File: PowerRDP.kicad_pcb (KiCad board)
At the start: 2 copper layers, 41.3 x 33.7 mm, 27 parts, among them J1 Conn_01x02_Male, J2 Conn_01x02_Male, J3 Conn_01x02_Male, J4 Conn_01x02_Male, J5 Conn_01x02_Male, J6 Conn_01x02_Male, J7 Conn_01x02_Male, J8 Conn_01x02_Male, J9 Conn_01x03_Male, U2 KA378R12C, U3 AZ1117CH-3.3, U4 MEA1D1515SC

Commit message: Increment revison
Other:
- board text added: "HELEN RDP Power Board Rev02"
- board text removed: "HELEN RDP Power Board Rev01"
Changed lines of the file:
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@@
     (arrow2b (pts (xy 120.65 39.37) (xy 121.776504 38.783579)))
   )
-  (gr_text "HELEN RDP Power Board Rev01" (at 137.16 71.12 90) (layer F.SilkS)
+  (gr_text "HELEN RDP Power Board Rev02" (at 140.97 69.85) (layer F.SilkS)
     (effects (font (size 0.8 0.8) (thickness 0.2)))
   )

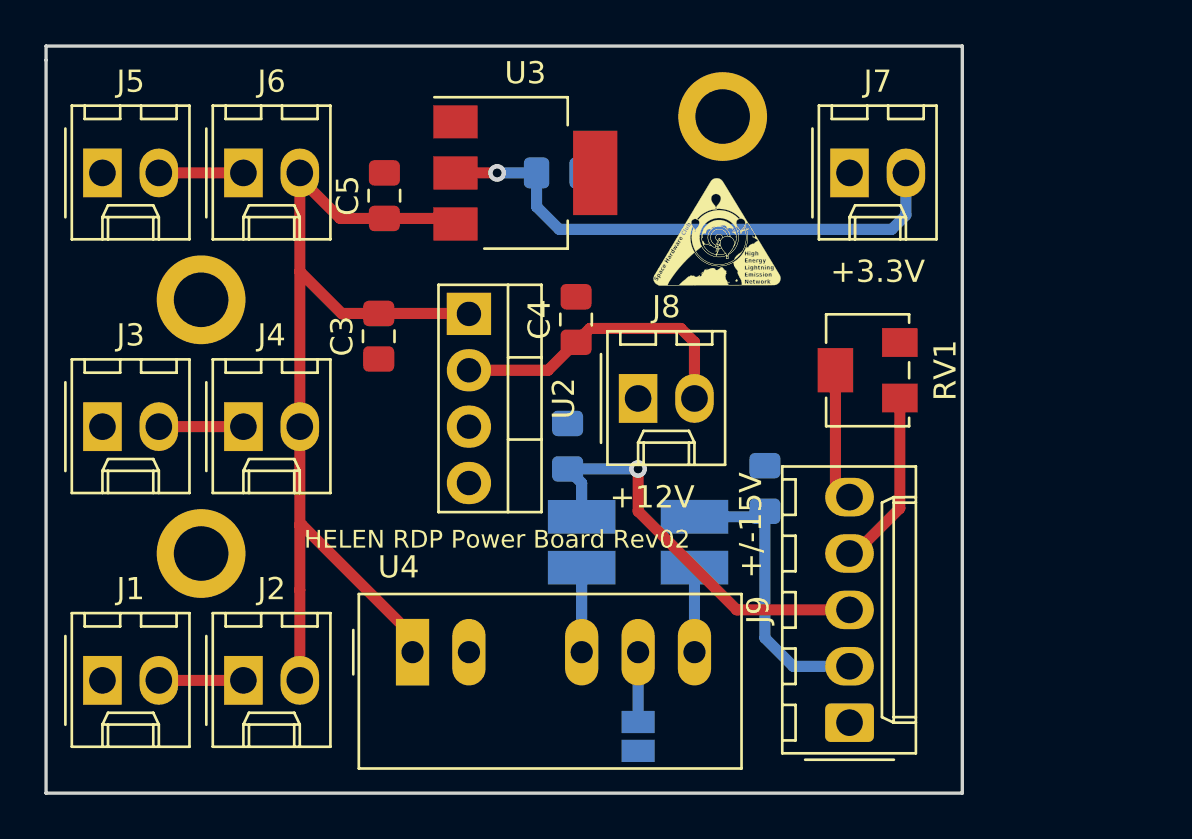
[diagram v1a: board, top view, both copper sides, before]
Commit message: Fix 15V regulator, add blinking FAA LEDs
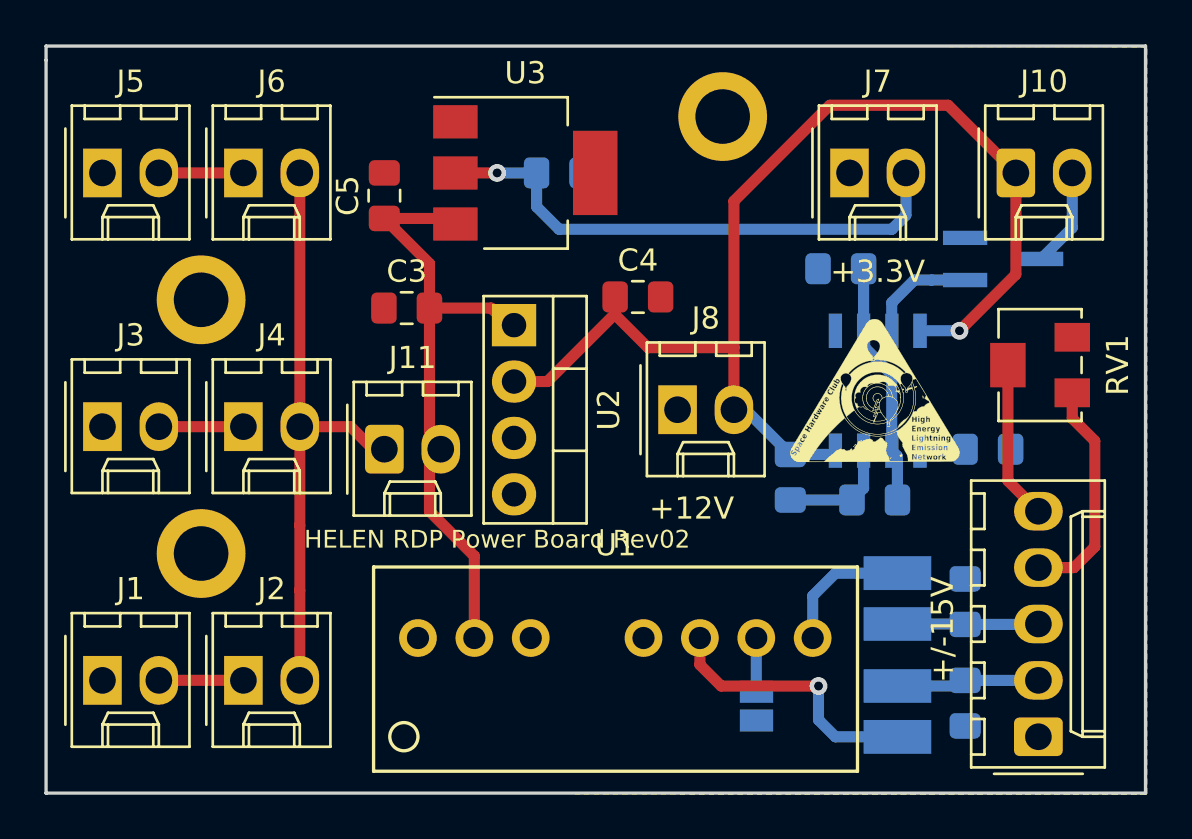
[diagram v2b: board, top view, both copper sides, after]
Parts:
- removed the G*** at (150.9, 55.9)
- added C7: .01 uF, Capacitor_SMD:C_0805_2012Metric_Pad1.15x1.40mm_HandSolder, B.Cu at (163.1, 65.8)
- added C8: 47 uF, Capacitor_SMD:C_0805_2012Metric_Pad1.15x1.40mm_HandSolder, B.Cu at (156.5, 57.7)
- added G***: LOGO, rdplibs:HELENlogo_large, F.Cu at (158.0, 63.0)
- added J10: FAA LED, Connector_Molex:Molex_KK-254_AE-6410-02A_1x02_P2.54mm_Vertical, F.Cu at (164.3, 53.3)
- added J11: Switch, Connector_Molex:Molex_KK-254_AE-6410-02A_1x02_P2.54mm_Vertical, F.Cu at (135.9, 65.8)
- added Q1: NTR4003NT1G, Package_TO_SOT_SMD:TSOT-23_HandSoldering, B.Cu at (163.8, 57.2)
- added R1: 3k, Resistor_SMD:R_0805_2012Metric_Pad1.15x1.40mm_HandSolder, B.Cu at (158.0, 68.1)
- added R2: 24k, Resistor_SMD:R_0805_2012Metric_Pad1.15x1.40mm_HandSolder, B.Cu at (154.2, 67.0)
- added U1: Recom_RS3, PowerRDP:Recom_RS3, F.Cu at (146.3, 75.7)
- J7: value Conn_01x02_Male -> 3.3V
- J8: value Conn_01x02_Male -> 12V
- J9: value Conn_01x03_Male -> FPGA
- U4: value MEA1D1515SC -> TS555; footprint Converter_DCDC:Converter_DCDC_TRACO_TMR-1-xxxx_Dual_THT -> Package_SO:SOIC-8_3.9x4.9mm_P1.27mm; moved to B.Cu
- moved U4 24.0 mm to (158.1, 63.2), turned to 270 degrees
- moved C1 19.2 mm to (162.1, 72.7)
- moved L1 14.4 mm to (159.0, 72.5), turned to 270 degrees
- moved C2 13.2 mm to (162.1, 77.2), turned to 270 degrees
- moved L2 11.9 mm to (159.0, 77.6)
- moved J9 8.53 mm to (165.4, 78.7)
- moved RV1 7.77 mm to (165.4, 62.0)
- moved JP1 5.51 mm to (152.7, 77.4)
- moved C4 2.96 mm to (147.3, 58.9), turned to 0 degrees
- moved U2 2.09 mm to (141.7, 60.2)
- moved J8 1.85 mm to (149.1, 64.0)
- moved C3 1.79 mm to (136.9, 59.4), turned to 0 degrees
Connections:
- C3 pad 2: +BATT -> /POWR
- C5 pad 1: +BATT -> /POWR
- U2 pad 1: +BATT -> /POWR
- U3 pad 3: +BATT -> /POWR
- U4 pad 1: +BATT -> GND
- U4 pad 2: GND -> /THR
- U4 pad 4: Net-(L1-Pad1) -> /+12V
- U4 pad 5: Net-(JP1-Pad1) -> Net-(C7-Pad1)
- U4 pad 6: Net-(L2-Pad1) -> /THR
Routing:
- net /+12V: track 13.7 -> 53.9 mm, vias 0 -> 1
- net /POWR: track 0.00 -> 27.8 mm
- net +BATT: track 70.1 -> 49.7 mm
- net /-15V: track 18.9 -> 6.36 mm, vias 1 -> 0
- net /THR: track 0.00 -> 11.0 mm
- net Net-(L2-Pad1): track 3.81 -> 12.3 mm, vias 0 -> 1
- net /+15V: track 13.3 -> 6.46 mm
- net Net-(R1-Pad1): track 0.00 -> 5.21 mm
- net /FAA_SIG: track 0.00 -> 5.00 mm
- net /FAA_GND: track 0.00 -> 4.46 mm
- net Net-(L1-Pad1): track 3.81 -> 6.14 mm
- net /C_in: track 8.08 -> 10.3 mm
- net Net-(C7-Pad1): track 0.00 -> 2.06 mm
- net /C_out: track 5.98 -> 7.15 mm
- net Net-(JP1-Pad1): track 3.14 -> 2.42 mm
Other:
- board size 41.3 x 33.7 mm -> 49.5 x 33.7 mm
- board text removed: "-"

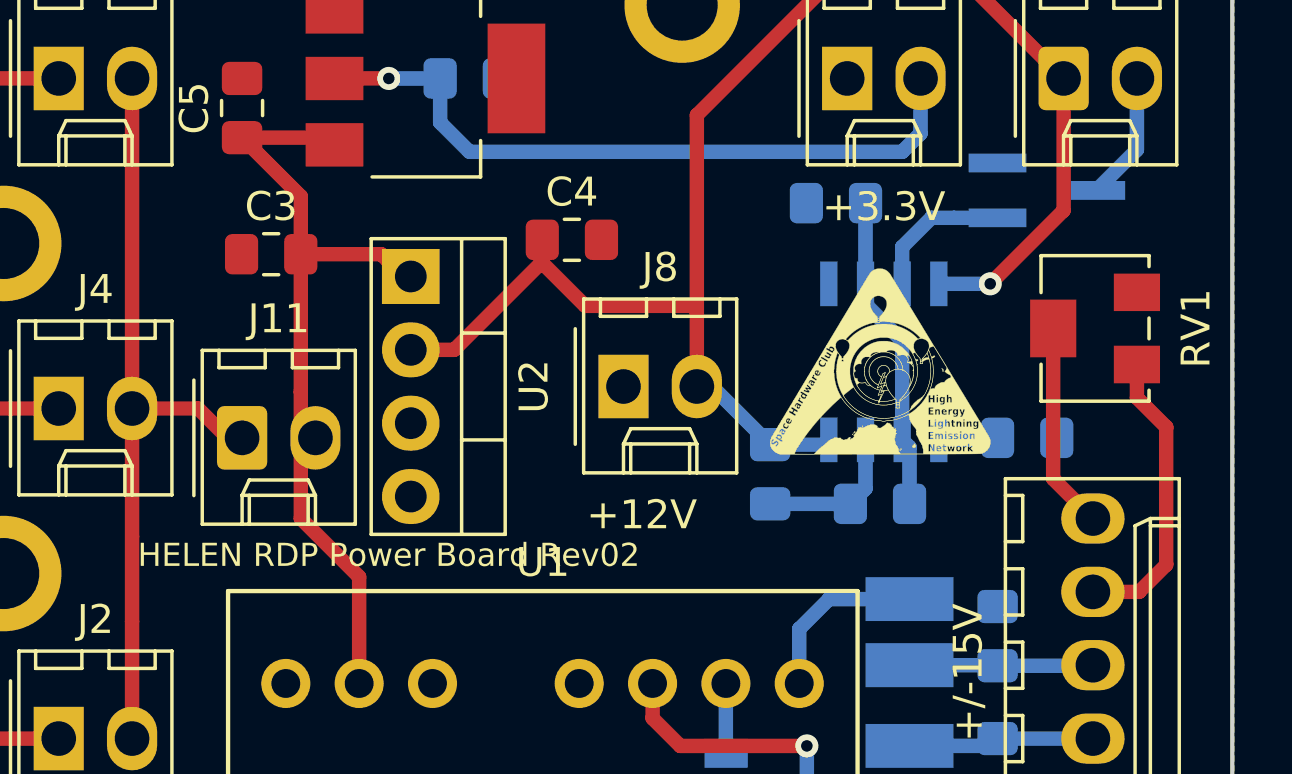
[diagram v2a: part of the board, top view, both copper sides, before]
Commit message: Add silkscreen labels to connectors
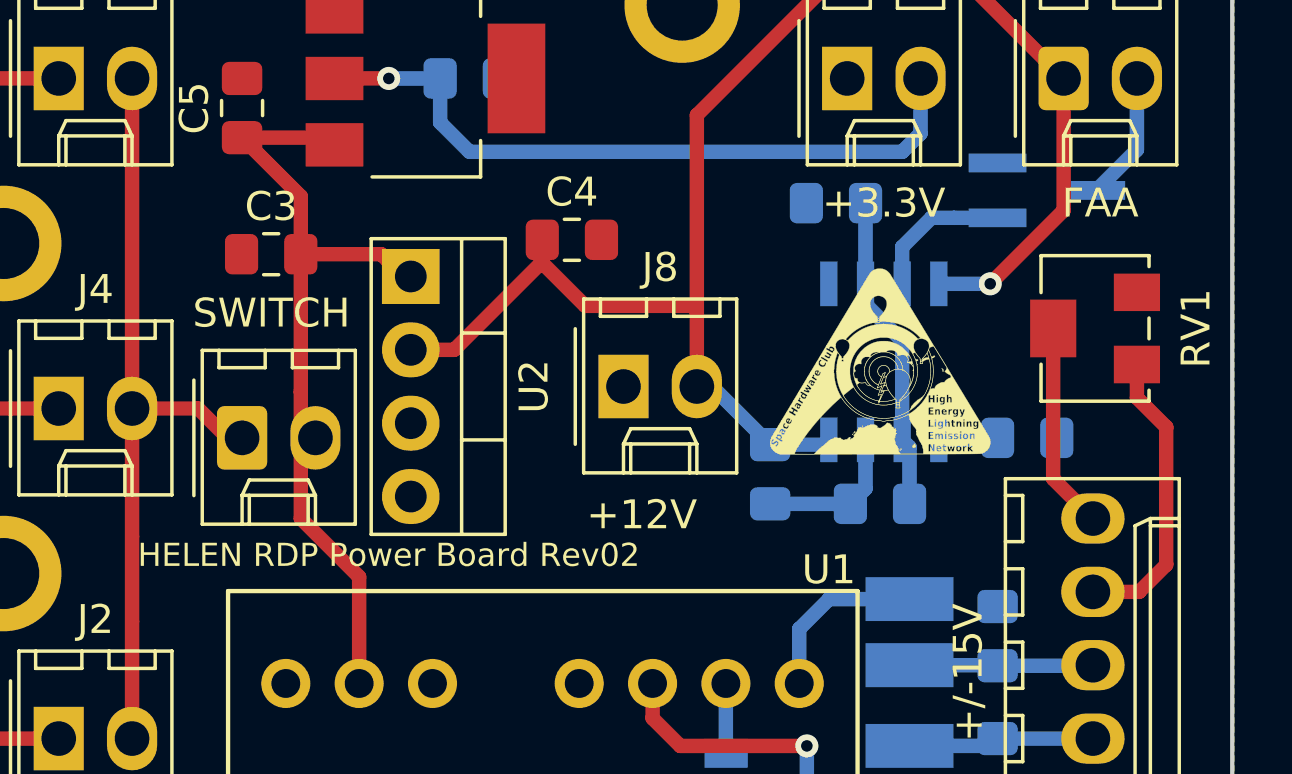
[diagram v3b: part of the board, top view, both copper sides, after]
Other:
- board text added: "FAA"
- board text added: "SWITCH"
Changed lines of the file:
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@@
   (general
     (thickness 1.6)
-    (drawings 16)
+    (drawings 18)
     (tracks 97)
     (zones 0)
@@
     (descr "Molex KK-254 Interconnect System, old/engineering part number: AE-6410-02A example for new part number: 22-27-2021, 2 Pins (http://www.molex.com/pdm_docs/sd/022272021_sd.pdf), generated with kicad-footprint-generator")
     (tags "connector Molex KK-254 side entry")
-    (fp_text reference J11 (at 1.27 -4.12) (layer F.SilkS)
+    (fp_text reference J11 (at 1.27 -4.12) (layer F.SilkS) hide
       (effects (font (size 1 1) (thickness 0.15)))
     )
@@
   (module PowerRDP:Recom_RS3 (layer F.Cu)
     (at 146.304 75.692)
-    (fp_text reference U1 (at 0 -5.588) (layer F.SilkS)
+    (fp_text reference U1 (at 9.906 -5.334) (layer F.SilkS)
       (effects (font (size 1 1) (thickness 0.15)))
     )
@@
       (xy 0.017454 -3.065725)) (layer F.SilkS) (width 0.01))
   )
+  (gr_text FAA (at 165.608 57.658) (layer F.SilkS)
+    (effects (font (size 1 1) (thickness 0.2)))
+  )
+  (gr_text "SWITCH\n" (at 136.906 61.468) (layer F.SilkS)
+    (effects (font (size 1 1) (thickness 0.2)))
+  )
   (gr_text + (at 168.402 75.946) (layer B.SilkS)
     (effects (font (size 1 1) (thickness 0.2)) (justify mirror))
@@
     (effects (font (size 1 1) (thickness 0.2)))
   )
-  (gr_text +3.3V (at 158.115 57.785) (layer F.SilkS)
+  (gr_text +3.3V (at 158.115 57.658) (layer F.SilkS)
     (effects (font (size 1 1) (thickness 0.2)))
   )

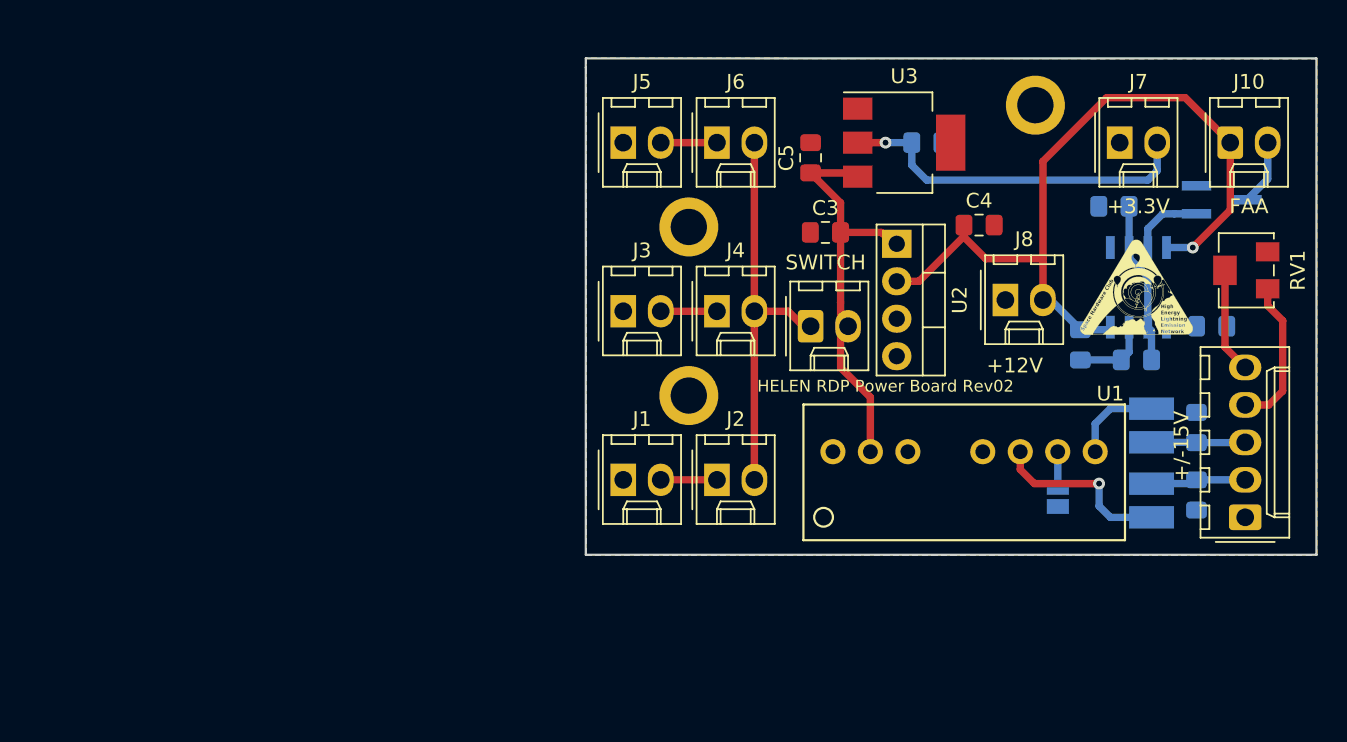
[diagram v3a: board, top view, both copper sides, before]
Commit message: Remake power board with updated single-output regulators. PCB entirely redesigned
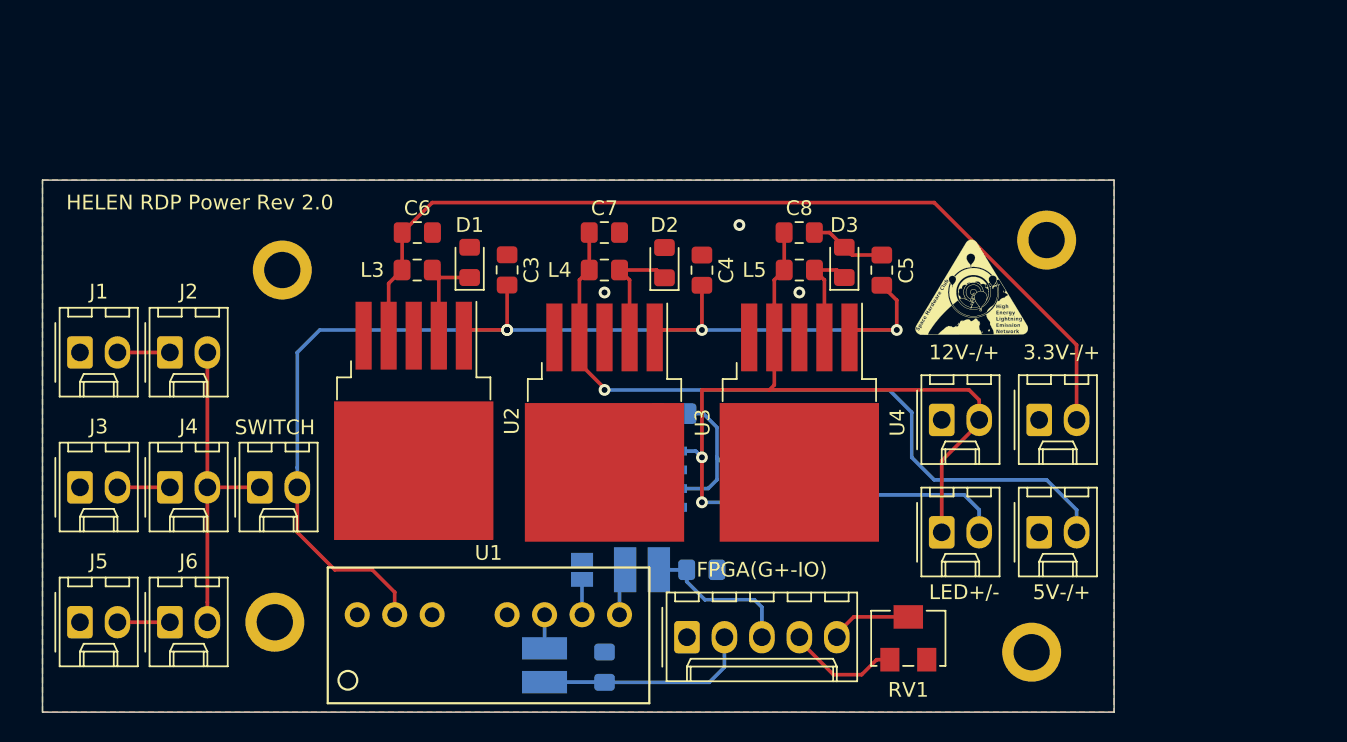
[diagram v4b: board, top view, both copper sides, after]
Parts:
- removed the G*** at (135.6, 62.7)
- removed the REF** at (151.1, 50.8)
- removed the REF** at (127.6, 70.5)
- removed the REF** at (127.6, 59.1)
- added C10: 47 uF, Capacitor_SMD:C_0805_2012Metric_Pad1.15x1.40mm_HandSolder, B.Cu at (126.6, 71.7)
- added C9: .01 uF, Capacitor_SMD:C_0805_2012Metric_Pad1.15x1.40mm_HandSolder, B.Cu at (123.4, 79.2)
- added D1: 1N5819, Diode_SMD:D_0805_2012Metric_Pad1.15x1.40mm_HandSolder, F.Cu at (112.8, 61.5)
- added D2: 1N5819, Diode_SMD:D_0805_2012Metric_Pad1.15x1.40mm_HandSolder, F.Cu at (126.0, 61.5)
- added D3: 1N5819, Diode_SMD:D_0805_2012Metric_Pad1.15x1.40mm_HandSolder, F.Cu at (138.2, 61.5)
- added G***: LOGO, rdplibs:GP2image, F.Cu at (103.6, 74.7)
- added J12: Switch, Connector_Molex:Molex_KK-254_AE-6410-02A_1x02_P2.54mm_Vertical, F.Cu at (98.6, 76.7)
- added L3: 330uH, Inductor_SMD:L_0805_2012Metric_Pad1.15x1.40mm_HandSolder, F.Cu at (109.2, 62.0)
- added L4: 330uH, Inductor_SMD:L_0805_2012Metric_Pad1.15x1.40mm_HandSolder, F.Cu at (121.9, 62.0)
- added L5: 330uH, Inductor_SMD:L_0805_2012Metric_Pad1.15x1.40mm_HandSolder, F.Cu at (135.1, 62.0)
- added REF**: ScrewHole, rdplibs:ScrewHole, F.Cu at (99.6, 85.9)
- added REF**: ScrewHole, rdplibs:ScrewHole, F.Cu at (100.1, 62.0)
- added REF**: ScrewHole, rdplibs:ScrewHole, F.Cu at (151.9, 59.9)
- added REF**: ScrewHole, rdplibs:ScrewHole, F.Cu at (150.9, 87.9)
- added U5: TS555, Package_SO:SOIC-8_3.9x4.9mm_P1.27mm, B.Cu at (129.4, 76.2)
- C3, C5: value 10 uF -> 100uF
- C4: value 47 uF -> 100uF
- C6: value 22 uF -> 330uF; moved to F.Cu
- C7: value .01 uF -> 330uF; moved to F.Cu
- C8: value 47 uF -> 330uF; moved to F.Cu
- J10: value FAA LED -> FPGA; footprint Connector_Molex:Molex_KK-254_AE-6410-02A_1x02_P2.54mm_Vertical -> Connector_Molex:Molex_KK-254_AE-6410-05A_1x05_P2.54mm_Vertical
- J11: value Switch -> FAA LED
- J8: value 12V -> 5V
- J9: value FPGA -> 12V; footprint Connector_Molex:Molex_KK-254_AE-6410-05A_1x05_P2.54mm_Vertical -> Connector_Molex:Molex_KK-254_AE-6410-02A_1x02_P2.54mm_Vertical
- U2: value KA378R12C -> LM2575-3.3BU; footprint Package_TO_SOT_THT:TO-220-4_Vertical -> Package_TO_SOT_SMD:TO-263-5_TabPin3
- U3: value AZ1117CH-3.3 -> LM2575-5.0BU; footprint Package_TO_SOT_SMD:SOT-223 -> Package_TO_SOT_SMD:TO-263-5_TabPin3
- U4: value TS555 -> LM2575-12BU; footprint Package_SO:SOIC-8_3.9x4.9mm_P1.27mm -> Package_TO_SOT_SMD:TO-263-5_TabPin3; moved to F.Cu
- moved J10 49.8 mm to (127.5, 86.9)
- moved J6 49.3 mm to (92.5, 85.9)
- moved J5 49.1 mm to (86.4, 85.9)
- moved L2 42.6 mm to (117.9, 88.8), turned to 270 degrees
- moved C2 41.8 mm to (121.9, 88.9), turned to 90 degrees
- moved C7 41.7 mm to (121.9, 59.4)
- moved J4 39.0 mm to (92.5, 76.7)
- moved J3 38.7 mm to (86.4, 76.7)
- moved J2 38.1 mm to (92.5, 67.6)
- moved J1 37.8 mm to (86.4, 67.6)
- moved L1 35.9 mm to (124.5, 82.3), turned to 0 degrees
- moved R2 35.7 mm to (119.4, 75.3), turned to 0 degrees
- moved R1 35.4 mm to (123.5, 76.3), turned to 270 degrees
- moved C6 35.1 mm to (109.2, 59.4)
- moved C1 34.9 mm to (128.5, 82.3), turned to 0 degrees
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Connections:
- C4 pad 1: /+12V -> GND
- C4 pad 2: GND -> /POWR
- C5 pad 1: /POWR -> GND
- C5 pad 2: GND -> /POWR
- C7 pad 1: Net-(C7-Pad1) -> /+5V
- C8 pad 1: /THR -> /+12V
- J10 pad 1: /+12V -> GND
- J10 pad 2: /FAA_GND -> /+15V
- J11 pad 1: +BATT -> /+12V
- J11 pad 2: /POWR -> /FAA_GND
- J8 pad 2: /+12V -> /+5V
- J9 pad 2: /+15V -> /+12V
- U2 pad 2: /+12V -> Net-(D1-Pad1)
- U2 pad 4: Net-(U2-Pad4) -> /+3.3V
- U3 pad 1: GND -> /POWR
- U3 pad 2: /+3.3V -> Net-(D2-Pad1)
- U3 pad 3: /POWR -> GND
- U3 pad 4: (no net) -> /+5V
- U4 pad 1: GND -> /POWR
- U4 pad 2: /THR -> Net-(D3-Pad1)
- U4 pad 3: /FAA_SIG -> GND
- U4 pad 5: Net-(C7-Pad1) -> GND
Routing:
- net /POWR: track 27.8 -> 82.7 mm, vias 0 -> 4
- net /+5V: track 0.00 -> 50.3 mm, vias 0 -> 1
- net /+3.3V: track 24.4 -> 63.0 mm, vias 1 -> 0
- net +BATT: track 49.7 -> 21.8 mm
- net Net-(L2-Pad1): track 12.3 -> 2.28 mm, vias 1 -> 0
- net /+12V: track 53.9 -> 63.4 mm, vias 1 -> 2
- net /+15V: track 6.46 -> 14.7 mm
- net /FAA_GND: track 4.46 -> 12.6 mm
- net Net-(D2-Pad1): track 0.00 -> 8.12 mm
- net Net-(D1-Pad1): track 0.00 -> 7.37 mm
- net Net-(D3-Pad1): track 0.00 -> 7.08 mm
- net GND: track 0.00 -> 5.20 mm, vias 0 -> 3
- net /THR: track 11.0 -> 15.3 mm
- net /-15V: track 6.36 -> 10.5 mm
- net Net-(L1-Pad1): track 6.14 -> 3.20 mm
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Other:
- board size 49.5 x 33.7 mm -> 72.6 x 36.1 mm
- net class Default: clearance 0.25 -> 0.2
- net class Larger removed
- rule pad_to_mask_clearance: 0.2 -> 0
- rule trace_clearance: 0.25 -> 0.2
- rule trace_min: 0.25 -> 0.2
- board text added: "12V-/+"
- board text added: "3.3V-/+"
- board text added: "5V-/+"
- board text added: "FPGA(G+-IO)"
- board text added: "HELEN RDP Power Rev 2.0"
- board text added: "LED+/-"
- board text removed: "+"
- board text removed: "+/-15V"
- board text removed: "+12V"
- board text removed: "+3.3V"
- board text removed: "FAA"
- board text removed: "G"
- board text removed: "HELEN RDP Power Board Rev02"

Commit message: Update diodes to something I can buy
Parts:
- D1, D2, D3: footprint Diode_SMD:D_0805_2012Metric_Pad1.15x1.40mm_HandSolder -> Diode_SMD:D_SOD-123
- moved D3 1.16 mm to (138.4, 60.3)
- moved D2 0.93 mm to (125.7, 60.6)
- moved D1 0.88 mm to (112.8, 60.6)
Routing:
- net Net-(D1-Pad1): track 7.37 -> 7.99 mm
